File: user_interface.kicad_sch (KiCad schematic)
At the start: 35 parts, among them CN5 Line out, CN6 Headphone, J2 SWD, J3 I2C, J6 SPI, J9 Serial, P1 GPIO, SW4 BTN1, SW5 BTN2

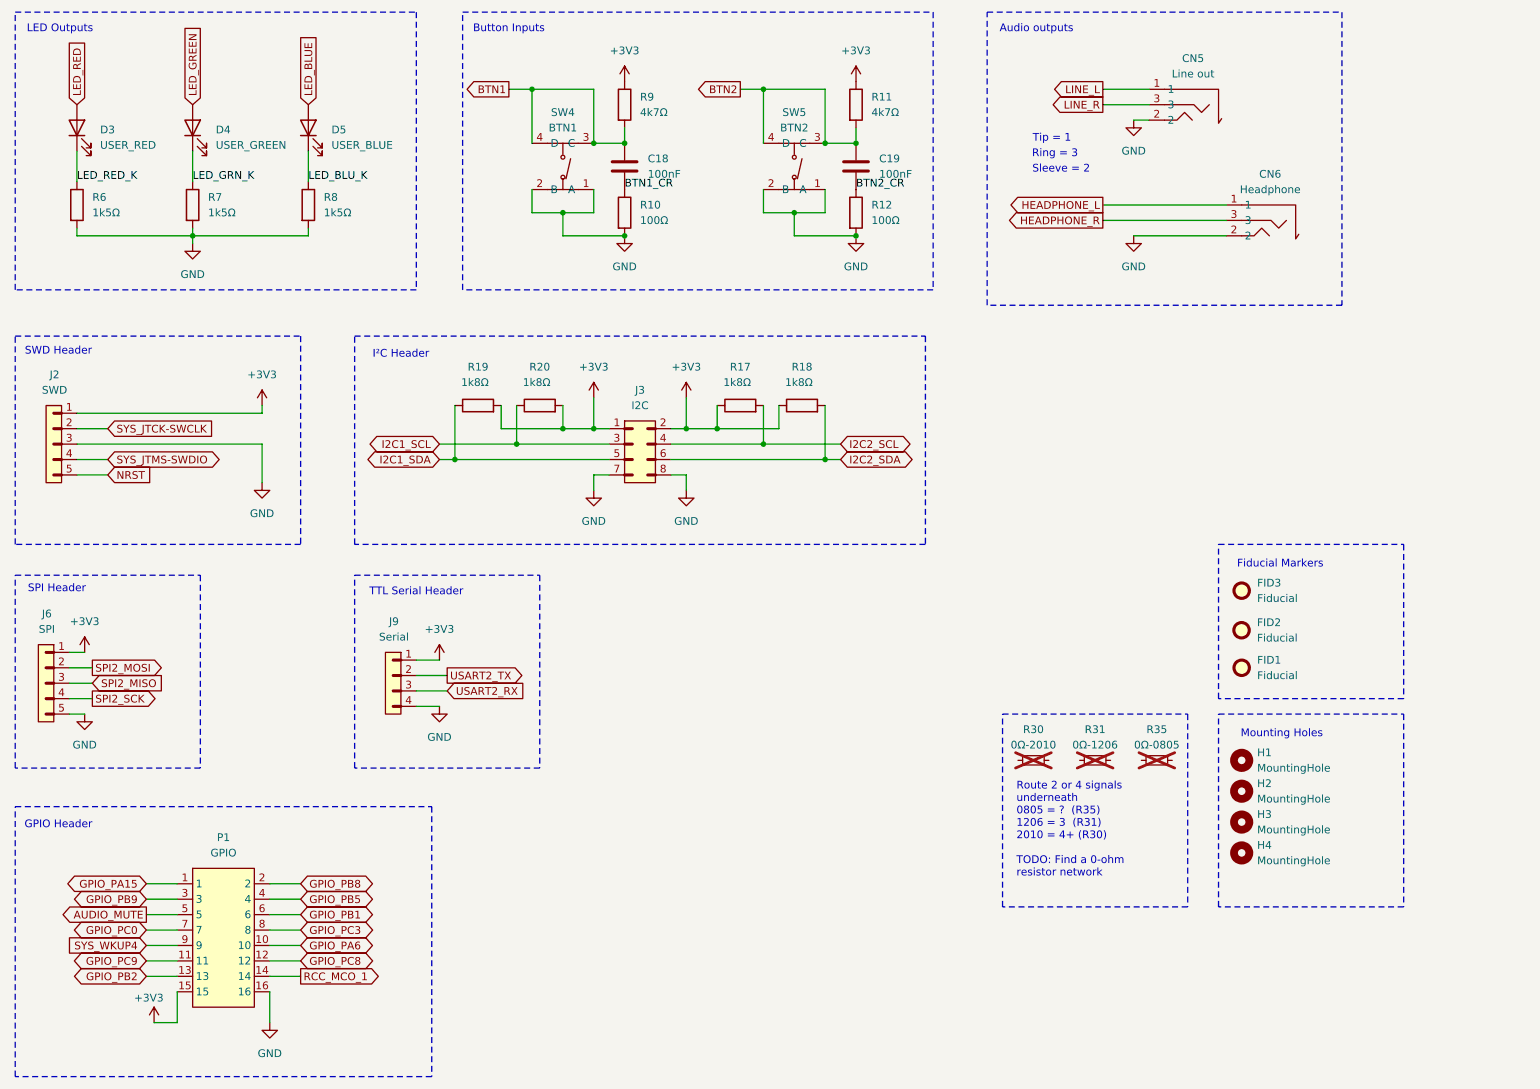
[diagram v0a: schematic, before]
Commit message: 1. Fixed mis-wired 3.5mm jacks everywhere. 2. Use smaller opto-isolator and diode with updated circuit for one MIDI.
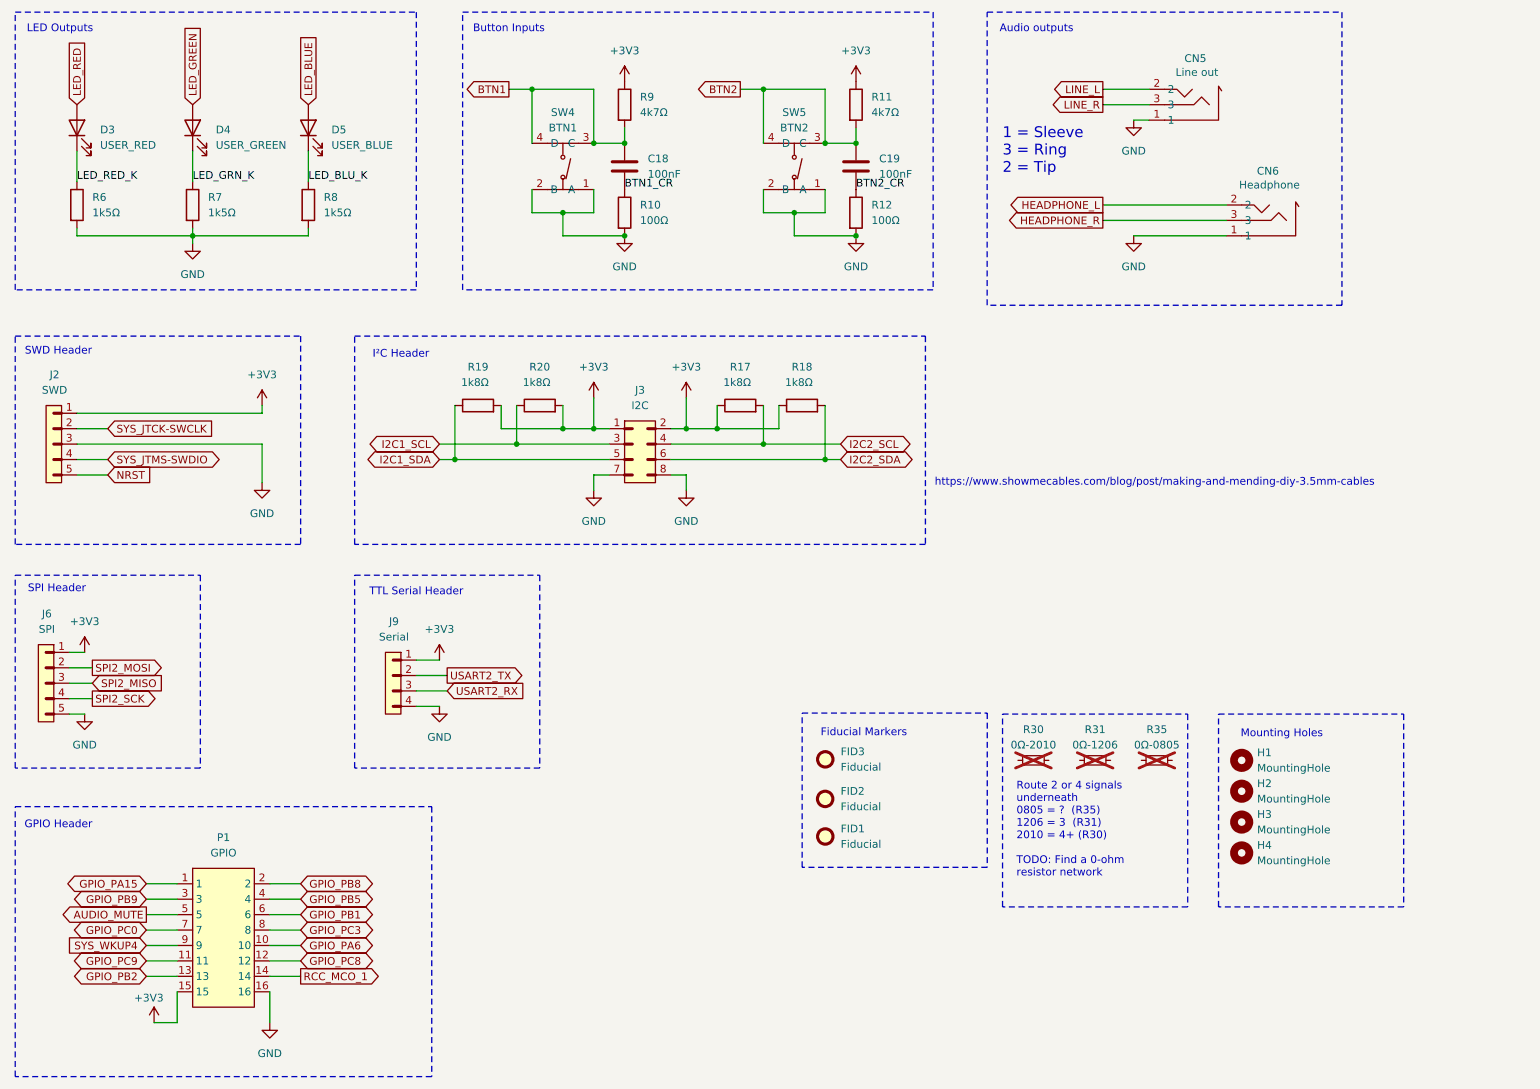
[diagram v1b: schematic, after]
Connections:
- net GND: now also CN5.1, CN6.1; no longer CN5.2, CN6.2
- net HEADPHONE_L: now also CN6.2; no longer CN6.1
- net LINE_L: now also CN5.2; no longer CN5.1
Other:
- note added: "1 = Sleeve 3 = Ring 2 = Tip"
- note added: "https://www.showmecables.com/blog/post/making-and-mending-diy-3.5mm-cables"
- note removed: "Ring = 3"
- note removed: "Sleeve = 2"
- note removed: "Tip = 1"
- moved on the sheet: CN5, CN6, FID1, FID2, FID3

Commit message: Continued additional minor cleanups
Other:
- note added: "Note: Buttons are high when not pressed"
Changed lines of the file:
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@@
+		)
+	)
+	(text "Note: Buttons are high when not pressed"
+		(exclude_from_sim no)
+		(at 127.508 63.246 0)
+		(effects
+			(font
+				(size 1.27 1.27)
+			)
 		)
 	)
@@
 					(size 1.27 1.27)
 				)
-			)
-		)
+				(hide yes)
+			)
+		)

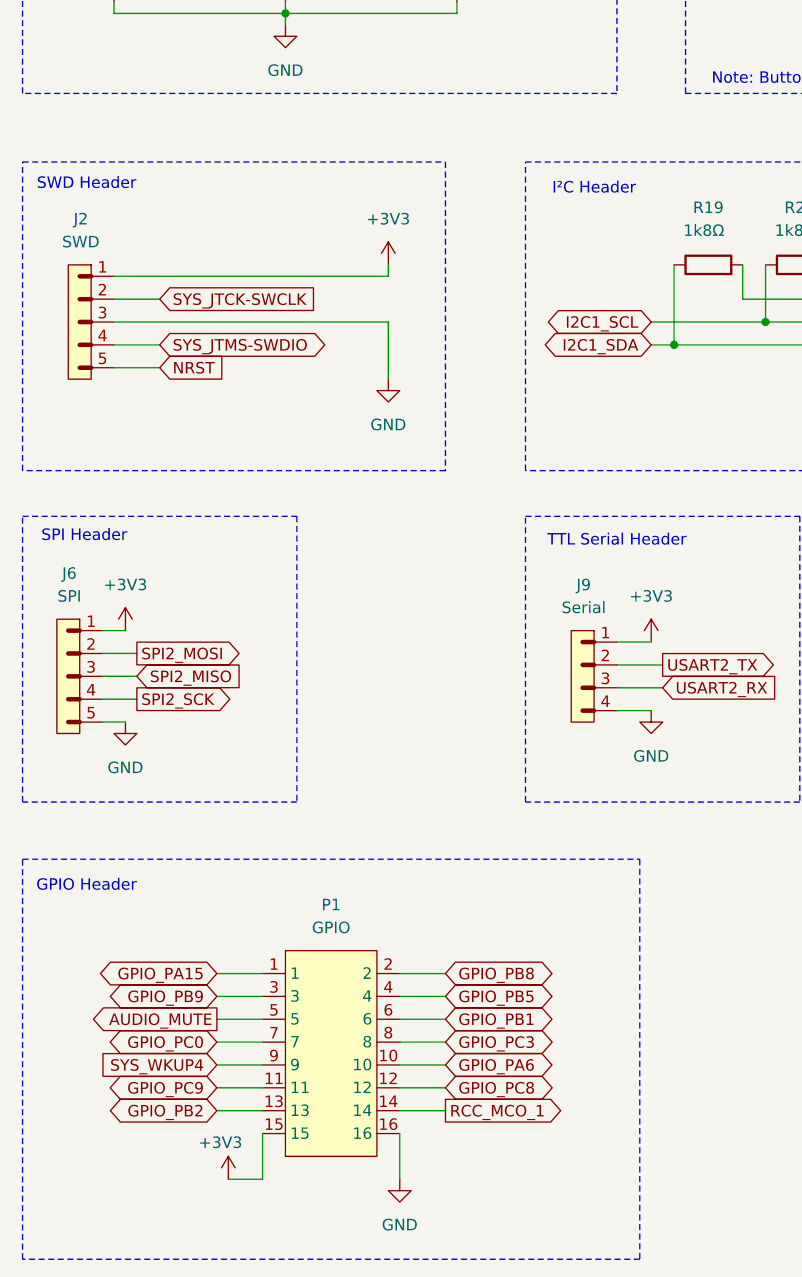
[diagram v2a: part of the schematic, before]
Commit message: More revisions for EVT2: 1. Move GAIN0/1 to MCU pins. 2. Revise SPI header with additional screen GPIO. 3. Revise GPIO header due to 1 and 2.
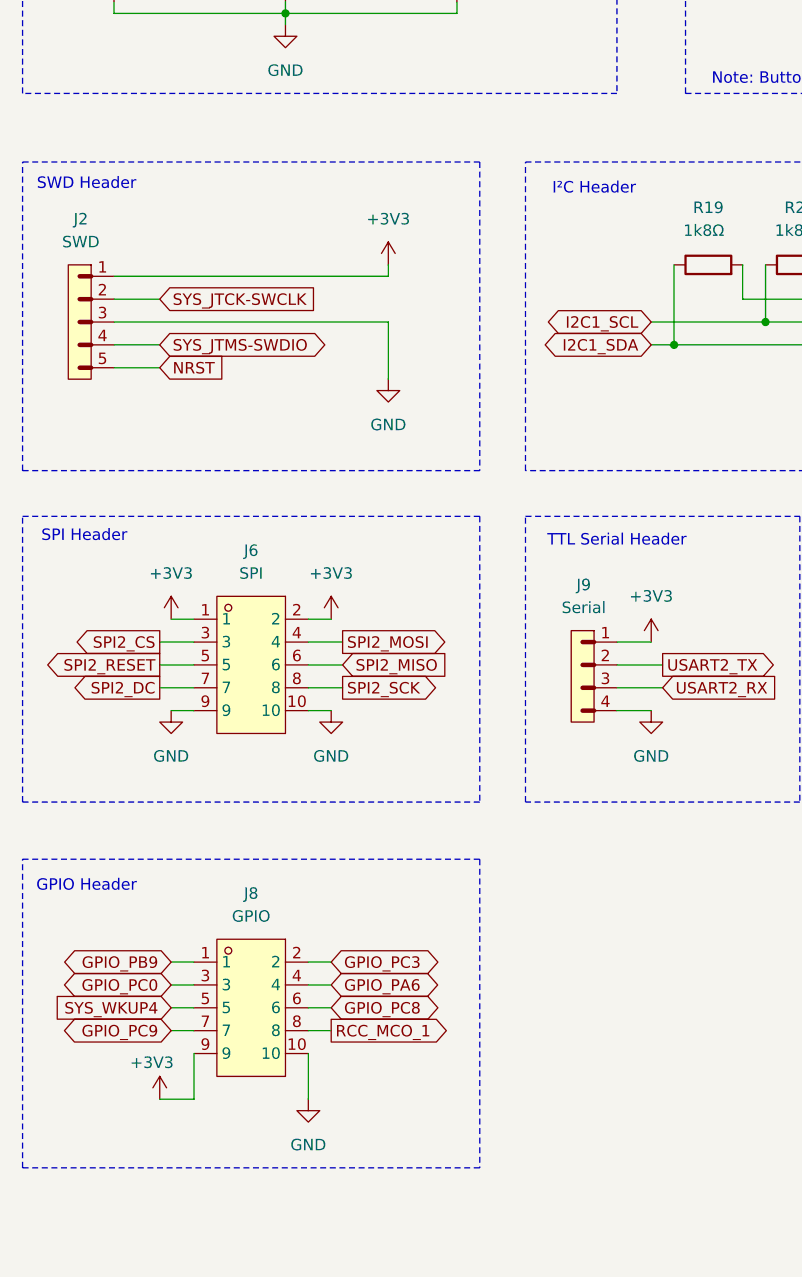
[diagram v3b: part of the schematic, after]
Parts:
- removed J6: SPI, Connector_PinHeader_2.54mm:PinHeader_1x05_P2.54mm_Vertical, symbol PCM_SL_Pin_Headers:PINHD_1x5_Male
- removed P1: GPIO, easyeda2kicad:HDR-TH_16P-P2.54-V-M-R2-C8-S2.54, symbol easyeda2kicad:Header-Male-2.54_2x8
- added J6: SPI, easyeda2kicad:HDR-TH_10P-P2.54-V-M-R2-C5-S2.54-1, symbol easyeda2kicad:PZ2.54-2*5
- added J8: GPIO, easyeda2kicad:HDR-TH_10P-P2.54-V-M-R2-C5-S2.54-1, symbol easyeda2kicad:PZ2.54-2*5
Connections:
- net +3V3: now also J6.1, J6.2, J8.9
- net GND: now also J6.10, J6.9, J8.10
- net GPIO_PA6: now also J8.4
- net GPIO_PB9: now also J8.1
- net GPIO_PC0: now also J8.3
- net GPIO_PC3: now also J8.2
- net GPIO_PC8: now also J8.6
- net GPIO_PC9: now also J8.7
- net RCC_MCO_1: now also J8.8
- net SPI2_MISO: now also J6.6
- net SPI2_MOSI: now also J6.4
- net SPI2_SCK: now also J6.8
- net SYS_WKUP4: now also J8.5
- new net SPI2_CS: J6.3
- new net SPI2_DC: J6.7
- new net SPI2_RESET: J6.5
